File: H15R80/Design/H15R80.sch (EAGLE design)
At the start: 49 parts, among them P1 HEXABIT_17.32_NO_P3_P6, U1 STM32F091CBU6, U2 DAC8760RHA, U3 OPA192, X1 XTALL_CSTCE8M00G52

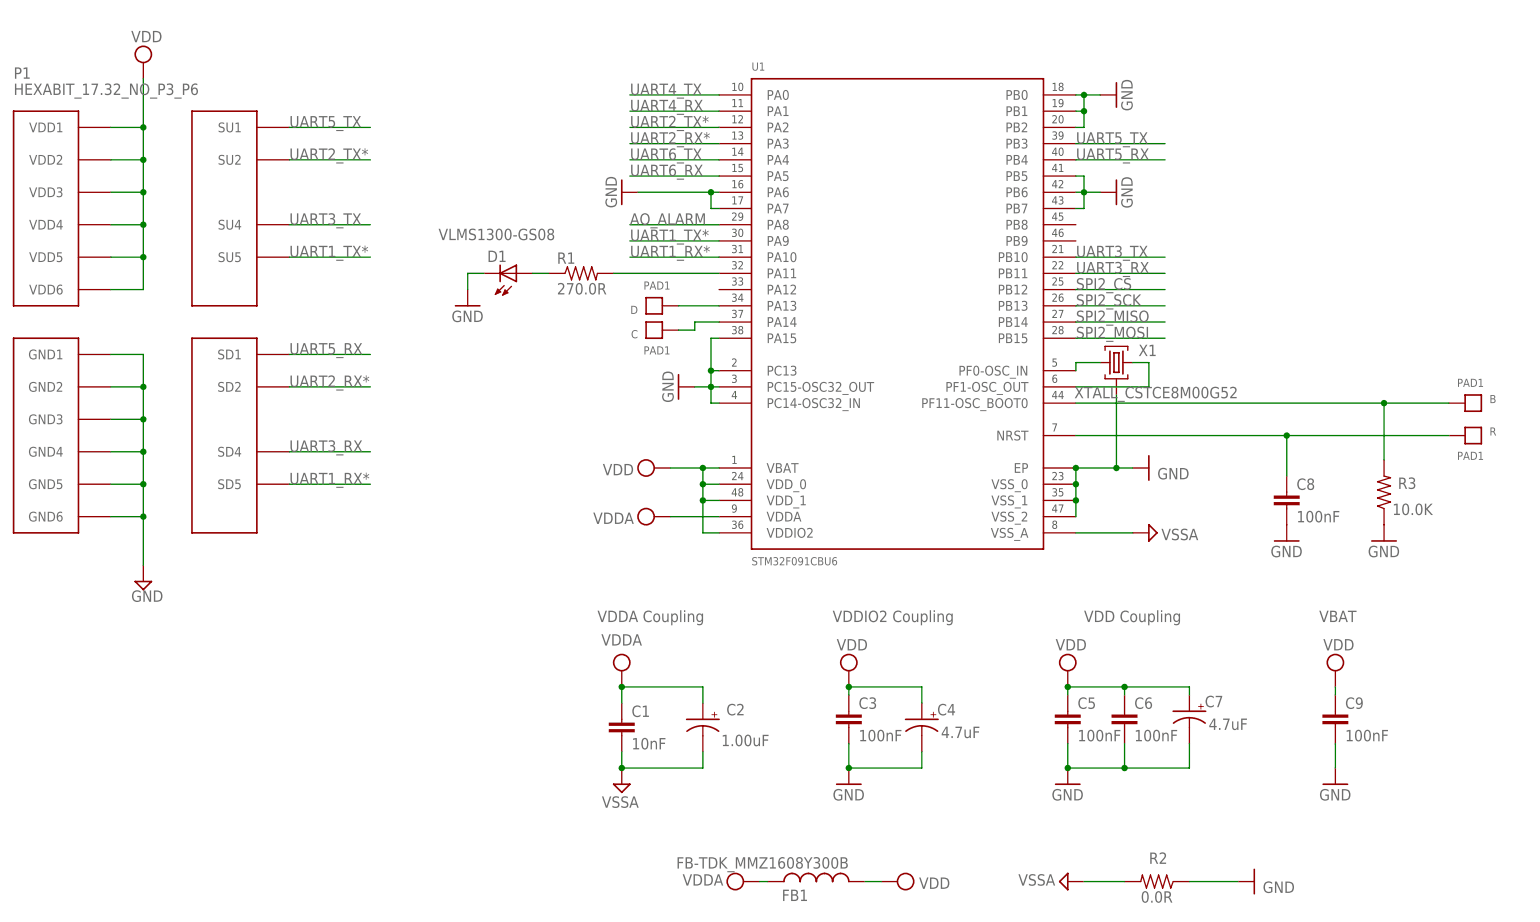
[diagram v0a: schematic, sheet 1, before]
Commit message: Changing MCU to STM32G0
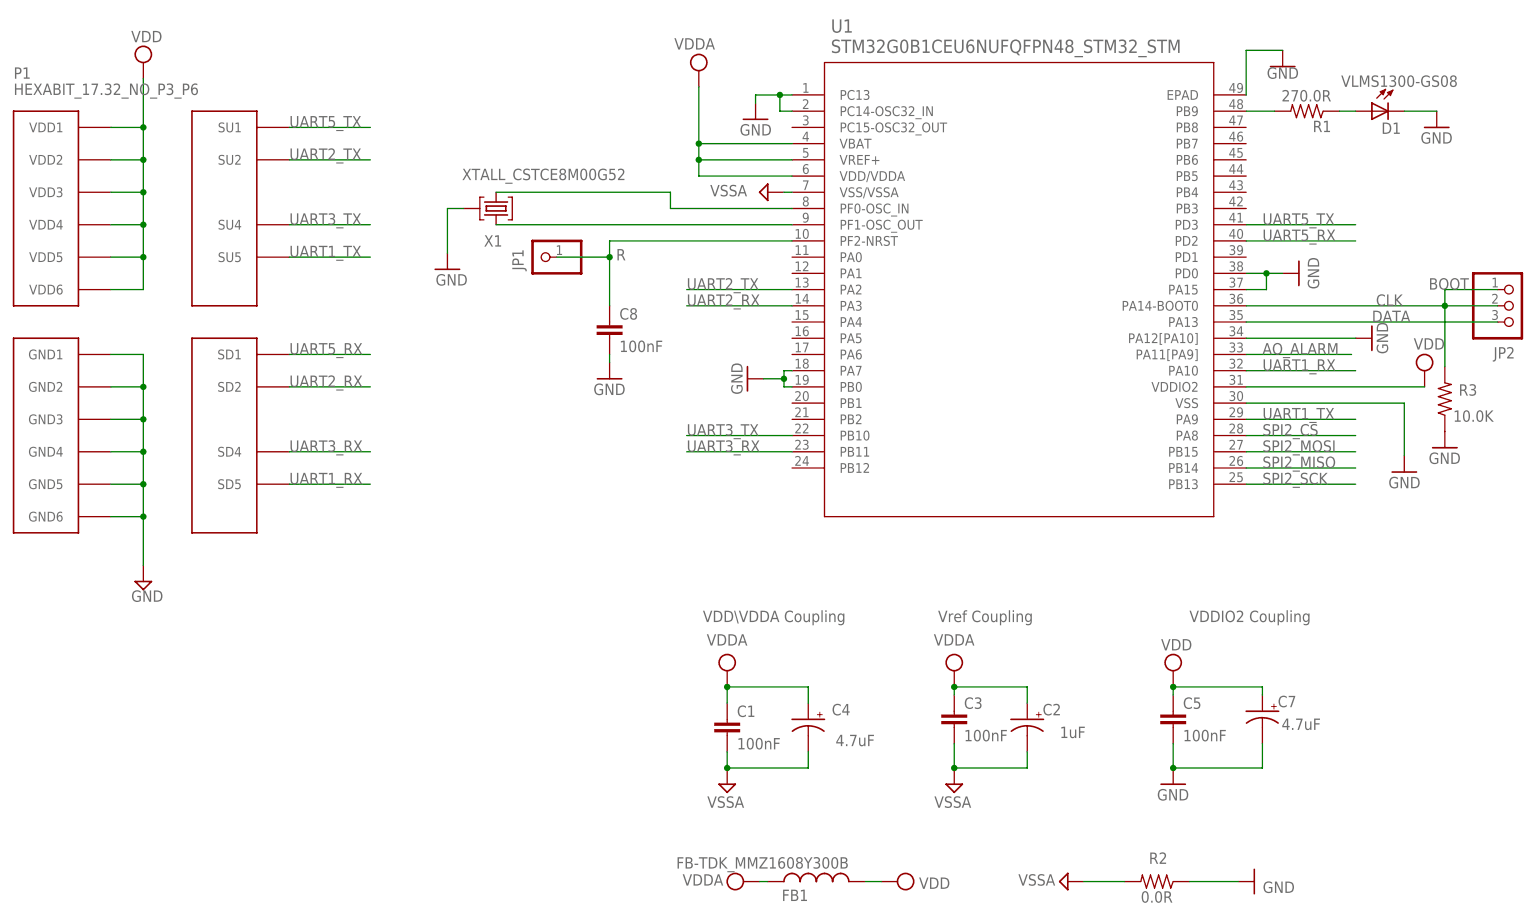
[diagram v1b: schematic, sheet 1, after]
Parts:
- removed B, C, D, R: PAD1, Hexabitz:PAD1
- removed C6, C9: 100nF, Hexabitz:C-0603
- added CS, MISO, MOSI, SCK: PAD4, HEXABITZ_CONNECTION_PARTS:PAD4
- added D2, D3: DIOD-SOD-123, HEXABITZ_RCLS:DIOD-SOD-123
- added F1, F2: NANOSMDC035F-2120, HEXABITZ_RCLS:NANOSMDC035F-2120
- added JP1: R, HEXABITZ_USER_INTERFACE_PARTS:PINHD-1X1
- added JP2: (no value), pinhead:PINHD-1X3
- added R4: 10R, Hexabitz:R-0603
- added TVS1, TVS2: SMBJ30CA, HEXABITZ_RCLS:SMBJ30CA
- C1: value 10nF -> 100nF
- C2: value 1.00uF -> 1uF; CAPACITANCE 1.00uF -> 4.7uF; MFN Yageo -> Murata; MPN CC0805KKX7R7BB105 -> GRM21BC81E475KA12L; OCTOPART_URL https://octopart.com/cc0805kkx7r7bb105-yageo-8376555?r=sp&s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 -> https://octopart.com/grm21bc81e475ka12l-murata-10331911?r=s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; VOLTAGE_RATING 16V -> 25V
- C4: CAPACITANCE 4.7uF -> 1.00uF; MFN Murata -> Yageo; MPN GRM21BC81E475KA12L -> CC0805KKX7R7BB105; OCTOPART_URL https://octopart.com/grm21bc81e475ka12l-murata-10331911?r=s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 -> https://octopart.com/cc0805kkx7r7bb105-yageo-8376555?r=sp&s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; VOLTAGE_RATING 25V -> 16V
- U1: value STM32F091CBU6 -> STM32G0B1CEU6NUFQFPN48_STM32_STM; device Hexabitz:STM32F091CBU6 -> HEXABITZ_ICs:STM32G0B1CEU6NUFQFPN48_STM32_STM
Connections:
- net UART1_RX* renamed UART1_RX
- net UART1_TX* renamed UART1_TX
- net UART2_RX* renamed UART2_RX
- net UART2_TX* renamed UART2_TX
- removed net B1: B.P$1, R3.2, U1.PF11-OSC_BOOT0
- removed net R1: C8.1, R.P$1, U1.NRST
- removed net UART4_RX: U1.PA1
- removed net UART4_TX: U1.PA0
- removed net UART6_RX: U1.PA5
- removed net UART6_TX: U1.PA4
- new net CLK: JP2.1, JP2.2, R3.2, U1.PA14-BOOT0
- new net DATA: JP2.3, U1.PA13
- new net N$12: F2.1, PWR-1.K
- new net N$15: D3.C, F2.2, TVS2.1
- new net N$16: D2.A, F1.2, TVS1.2
- new net N$17: D2.C, R4.2
- net +15V: now also R4.1; no longer PWR-3.K
- net -15V: now also D3.A; no longer PWR-1.K
- net AO_ALARM: now also U1.PA11[PA9]; no longer U1.PA8
- net GND: now also U1.EPAD, U1.PA12[PA10], U1.PD0, U1.VSS; no longer C3.2, C4.-, C6.2, C9.2, U1.EP, U1.PA6, U1.PB1, U1.PB2, U1.PB5, U1.PB6, U1.PB7, U1.PC15-OSC32_OUT, U1.VSS_0, U1.VSS_1, U1.VSS_2
- net N$3: now also U1.PB9; no longer U1.PA11
- net N$5: now also C8.1, JP1.1, U1.PF2-NRST; no longer U1.PF0-OSC_IN, X1.1
- net N$6: now also X1.1; no longer X1.3
- net N$7: now also U1.PF0-OSC_IN, X1.3; no longer D.P$1, U1.PA13
- net N$9: now also F1.1, PWR-3.K; no longer C.P$1, U1.PA14
- net SPI2_CS: now also CS.P$1, U1.PA8; no longer U1.PB12
- net SPI2_MISO: now also MISO.P$1
- net SPI2_MOSI: now also MOSI.P$1
- net SPI2_SCK: now also SCK.P$1
- net UART5_RX: now also U1.PD2; no longer U1.PB4
- net UART5_TX: now also U1.PD3; no longer U1.PB3
- net VDD: no longer C3.1, C4.+, C6.1, C9.1, U1.VBAT, U1.VDD_0, U1.VDD_1
- net VDDA: now also C3.1, C4.+, U1.VBAT, U1.VDD/VDDA, U1.VREF+; no longer U1.VDDA
- net VSSA: now also C3.2, C4.-, TVS1.1, TVS2.2, U1.VSS/VSSA; no longer U1.VSS_A
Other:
- note added: "BOOT"
- note added: "Obada Albasha"
- note added: "VDD\VDDA Coupling"
- note added: "Vref Coupling"
- note removed: "VBAT"
- note removed: "VDD Coupling"
- note removed: "VDDA Coupling"
- moved on the sheet: C1, C2, C3, C4, C5, C7, C8, D1, PWR-1, PWR-2, PWR-3, R1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

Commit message: Replace the blind vias with through hole ones
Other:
- note added: "VDD = 3.3 Volts"
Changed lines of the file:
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@@
 <text x="247.015" y="147.32" size="1.778" layer="95">BOOT</text>
 <text x="182.8292" y="5.0292" size="1.9304" layer="101" font="vector">Obada Albasha</text>
+<text x="43.815" y="191.135" size="1.778" layer="102">VDD = 3.3 Volts</text>
 </plain>
 <instances>
